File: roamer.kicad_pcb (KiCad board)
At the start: 4 copper layers, 108 parts, among them J1 Conn_Coaxial_Small, J2 JSTPH, J3 Conn_02x05_Odd_Even, J4 Conn_Coaxial_Small, J8 MEM2075-00-140-01-A, Q3 DMP2070UQ-7, SW1 KMR2, U1 2MB Flash, U2 AP2112K-3.3, U3 MCP73831-2-OT, U4 RFM95W-915S2, U5 RFM69W, U6 AP3602AKTR-G1, U7 BME688, U8 INA260, X2 32.768 kHz, X3 microUSB 2.0 B

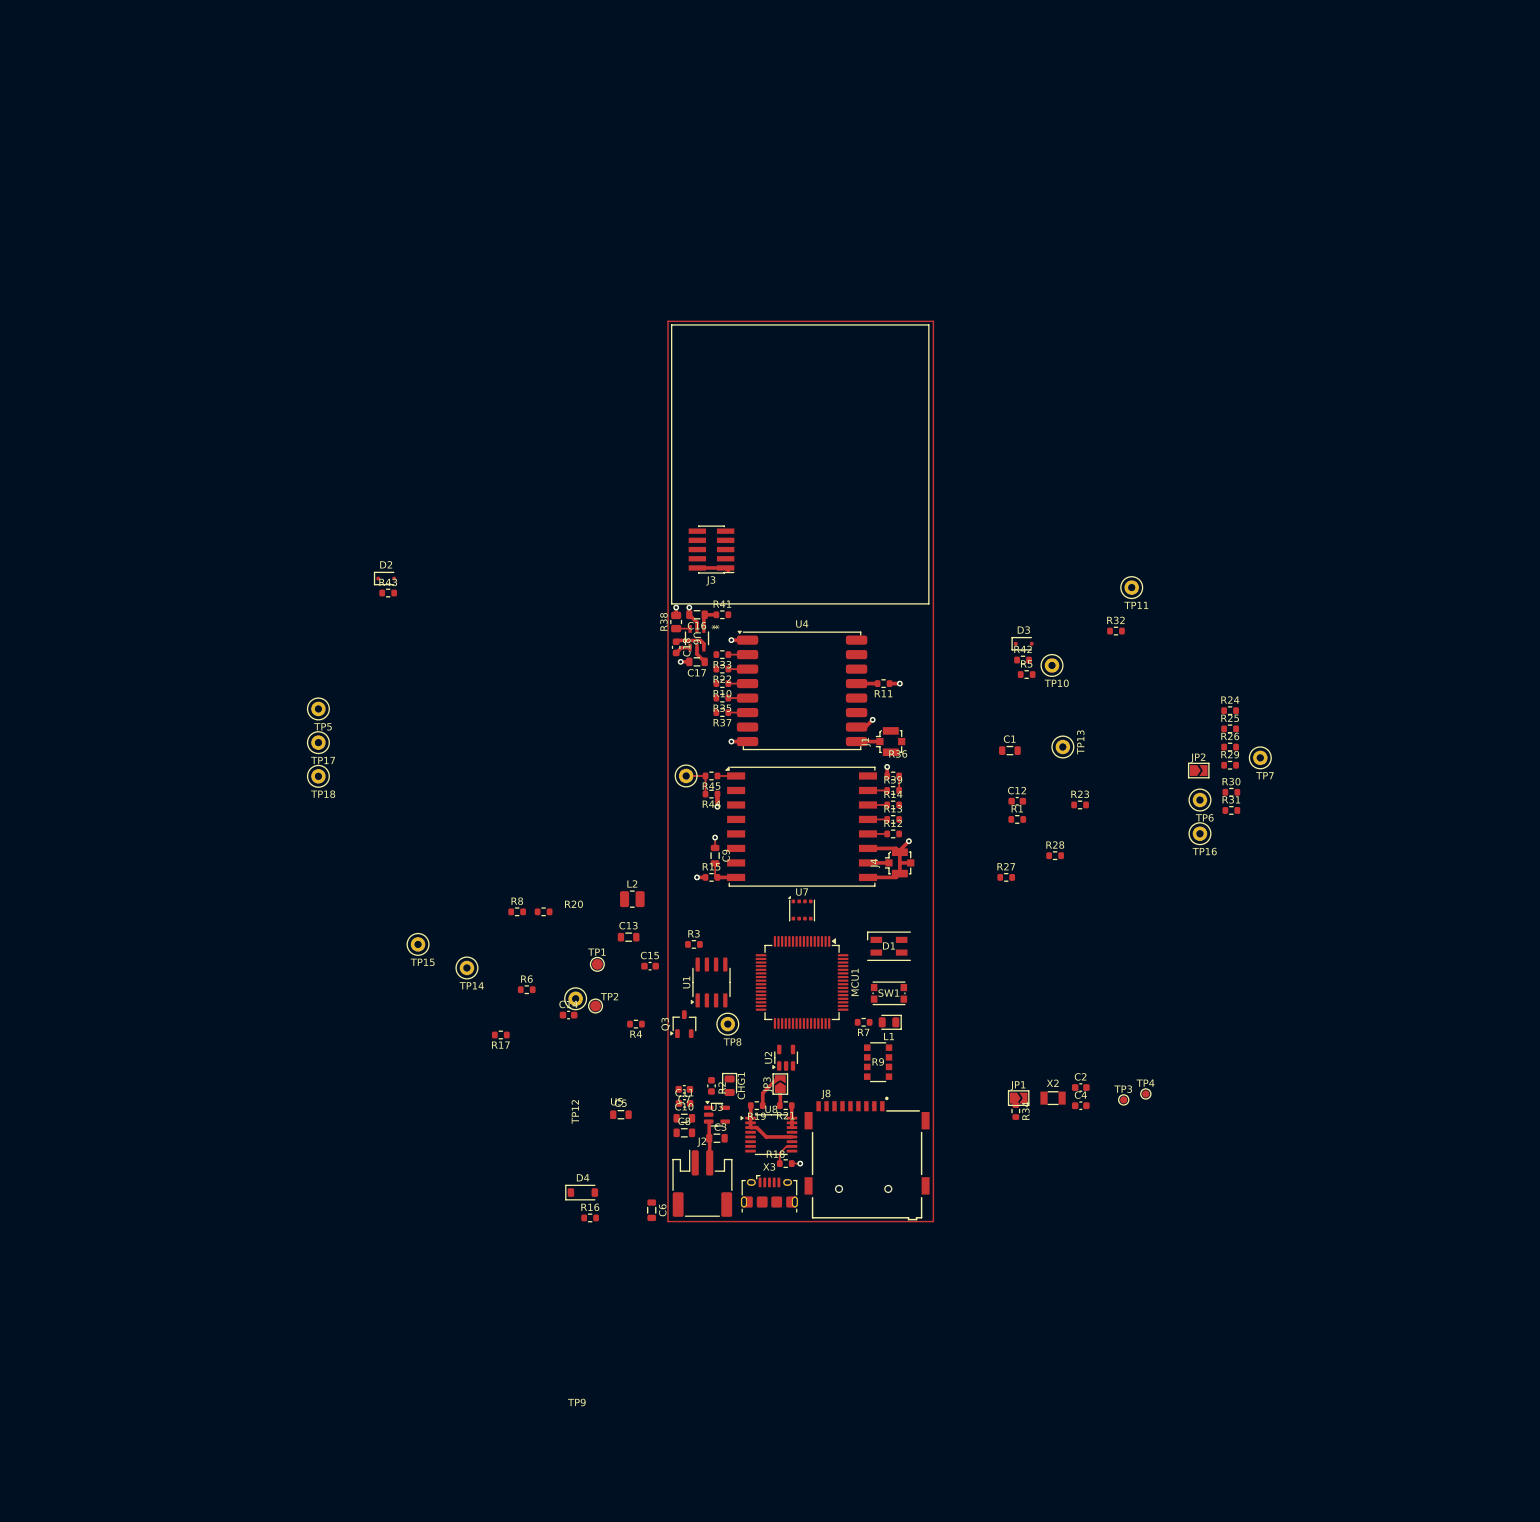
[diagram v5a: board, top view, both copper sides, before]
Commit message: Layed out the radio and PMS00
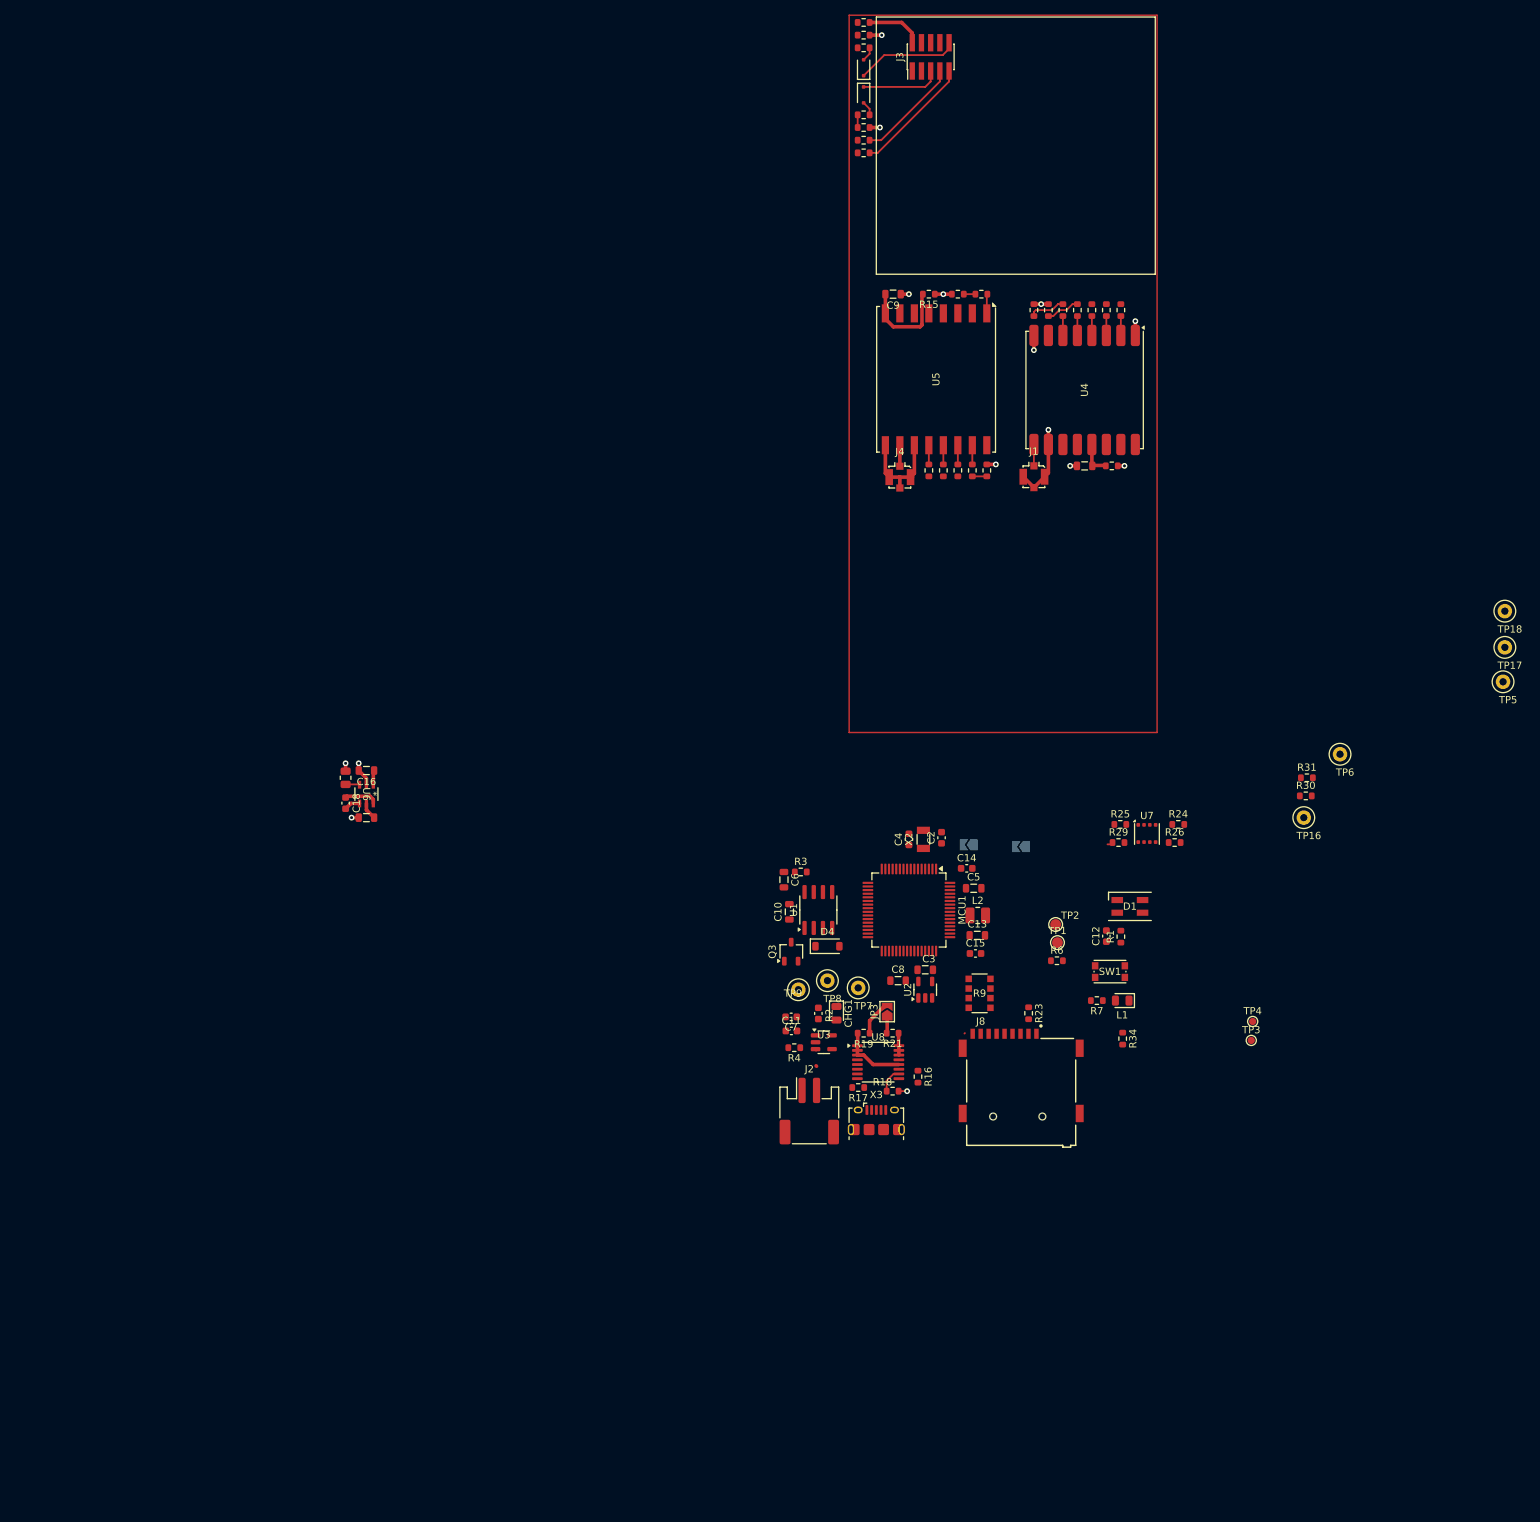
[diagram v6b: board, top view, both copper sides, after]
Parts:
- removed TP10, TP11, TP12, TP13, TP14, TP15: TestPoint, TestPoint:TestPoint_Loop_D2.50mm_Drill1.0mm
- JP1, JP2: moved to B.Cu
- moved TP18 165.3 mm to (307.0, 115.8)
- moved TP17 164.3 mm to (307.0, 120.8)
- moved TP5 163.5 mm to (306.8, 125.5)
- moved R8 110.8 mm to (244.0, 74.2), turned to -90 degrees
- moved R20 107.1 mm to (242.0, 74.2), turned to -90 degrees
- moved R27 103.6 mm to (218.5, 50.8), turned to 180 degrees
- moved R28 100.5 mm to (218.5, 52.5), turned to 180 degrees
- moved D2 93.8 mm to (218.5, 44.5), turned to -90 degrees
- moved R43 93.1 mm to (218.5, 47.2), turned to 180 degrees
- moved R5 91.1 mm to (218.5, 36.2), turned to 180 degrees
- moved R42 87.3 mm to (218.5, 38.0)
- moved R15 85.9 mm to (227.5, 72.0), turned to 180 degrees
- moved R41 84.0 mm to (218.5, 34.5)
- moved D3 82.5 mm to (218.5, 40.8), turned to 90 degrees
- moved C9 81.3 mm to (222.6, 72.0), turned to 180 degrees
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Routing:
- net Net-(J3-Pin_9): track 0.00 -> 16.5 mm
- net Net-(J3-Pin_7): track 0.00 -> 14.5 mm
- net Net-(D3-K): track 0.00 -> 14.2 mm
- net Net-(D2-K): track 0.00 -> 11.0 mm
- net Net-(U5-3.3V): track 4.90 -> 13.3 mm
- net GND: track 28.8 -> 35.4 mm
- net +BATT: track 11.0 -> 5.43 mm
- net /Comms - LoRa 900/~{RESET_LORA_900}: track 0.00 -> 5.02 mm
- net /Comms - LoRa 900/CS_LORA_900: track 0.00 -> 4.68 mm
- net +3V3: track 10.3 -> 14.7 mm, vias 6 -> 8
- net /Comms - LoRa 433/~{RESET_LORA_433}: track 5.18 -> 1.60 mm
- net Net-(J3-Pin_1): track 4.43 -> 7.83 mm
- net Net-(U4-3.3V): track 2.90 -> 5.02 mm
- net Net-(D3-A): track 0.00 -> 1.99 mm
- net Net-(D2-A): track 0.00 -> 1.99 mm
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
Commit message: Working on layout still
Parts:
- added R5: 10K, Resistor_SMD:R_0603_1608Metric, F.Cu at (255.5, 101.8)
- added TP10: TestPoint, TestPoint:TestPoint_Loop_D2.50mm_Drill1.0mm, F.Cu at (245.2, 50.4)
- added TP11: TestPoint, TestPoint:TestPoint_Loop_D2.50mm_Drill1.0mm, F.Cu at (245.2, 55.0)
- added TP12: TestPoint, TestPoint:TestPoint_Loop_D2.50mm_Drill1.0mm, F.Cu at (238.5, 50.4)
- added TP13: TestPoint, TestPoint:TestPoint_Loop_D2.50mm_Drill1.0mm, F.Cu at (238.5, 55.0)
- added TP14: TestPoint, TestPoint:TestPoint_Loop_D2.50mm_Drill1.0mm, F.Cu at (251.8, 50.4)
- added TP15: TestPoint, TestPoint:TestPoint_Loop_D2.50mm_Drill1.0mm, F.Cu at (251.8, 55.0)
- moved C17 89.6 mm to (228.2, 100.8), turned to -90 degrees
- moved C18 88.2 mm to (226.2, 103.6), turned to 180 degrees
- moved TP18 86.2 mm to (238.5, 63.5), turned to 90 degrees
- moved TP17 85.5 mm to (243.5, 63.5), turned to 90 degrees
- moved U6 85.2 mm to (225.0, 100.8), turned to 0 degrees
- moved TP5 85.1 mm to (248.2, 63.8), turned to 90 degrees
- moved R38 83.5 mm to (222.8, 103.6), turned to 180 degrees
- moved C16 80.8 mm to (221.8, 100.8), turned to -90 degrees
- moved C10 77.0 mm to (252.5, 94.2), turned to 0 degrees
- moved R18 75.7 mm to (236.7, 107.6), turned to 90 degrees
- moved U1 71.3 mm to (252.2, 98.0), turned to 180 degrees
- moved R19 68.4 mm to (235.0, 107.6), turned to 90 degrees
- moved U8 66.3 mm to (234.8, 113.2), turned to 90 degrees
- moved U3 64.7 mm to (227.7, 112.2), turned to 180 degrees
- moved R4 63.7 mm to (227.3, 115.0)
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- renumbered R5 to R40
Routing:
- net Net-(D3-K): track 14.2 -> 51.0 mm, vias 0 -> 2
- net Net-(J3-Pin_9): track 16.5 -> 51.6 mm, vias 0 -> 2
- net Net-(J3-Pin_7): track 14.5 -> 49.3 mm, vias 0 -> 2
- net +5V: track 2.24 -> 34.8 mm, vias 0 -> 2
- net Net-(D2-K): track 11.0 -> 42.4 mm, vias 0 -> 2
- net Net-(J3-Pin_1): track 7.83 -> 34.5 mm
- net GND: track 35.4 -> 58.2 mm, vias 7 -> 14
- net +3V3: track 14.7 -> 37.2 mm, vias 8 -> 11
- net /MCU/AIRQ_SET: track 0.10 -> 16.8 mm
- net Net-(D4-K): track 0.00 -> 16.0 mm
- net /MCU - Memory/QSPI.DATA0: track 0.00 -> 8.77 mm, vias 0 -> 3
- net Net-(U8-VBUS): track 9.30 -> 1.99 mm
- net /MCU - Memory/QSPI.SCK: track 0.00 -> 7.25 mm
- net /MCU - Memory/QSPI.DATA2: track 0.00 -> 6.93 mm
- net /MCU/~{AIRQ_RESET}: track 1.75 -> 8.58 mm
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
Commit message: Getting there with the layout
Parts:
- removed TP10, TP11, TP12, TP13, TP14, TP15, TP7, TP8, TP9: TestPoint, TestPoint:TestPoint_Loop_D2.50mm_Drill1.0mm
- JP3: moved to B.Cu
- moved C6 58.4 mm to (189.1, 157.0)
- moved D4 58.4 mm to (194.1, 156.8)
- moved Q3 58.4 mm to (189.1, 160.0)
- moved R3 58.4 mm to (190.0, 162.8)
- moved R4 58.4 mm to (193.8, 162.8)
- moved U2 58.4 mm to (194.1, 165.5)
- moved U3 58.4 mm to (194.1, 160.0)
- moved CHG1 52.9 mm to (186.5, 166.8), turned to 0 degrees
- moved R18 52.3 mm to (219.1, 156.9), turned to -90 degrees
- moved R34 52.1 mm to (216.1, 159.4)
- moved J8 51.9 mm to (223.1, 172.7)
- moved R17 51.8 mm to (217.1, 149.4), turned to 90 degrees
- moved R19 51.2 mm to (220.9, 156.9), turned to -90 degrees
- moved R16 50.5 mm to (217.1, 153.4)
- moved TP6 49.7 mm to (206.4, 151.4)
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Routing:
- net /Bus - SPI/SPI.SCK: track 0.00 -> 82.7 mm, vias 0 -> 4
- net /Bus - SPI/SPI.MISO: track 0.00 -> 69.8 mm, vias 0 -> 4
- net /Bus - SPI/SPI.MOSI: track 0.39 -> 68.5 mm, vias 0 -> 4
- net /Comms - LoRa 433/~{RESET_LORA_433}: track 1.60 -> 47.8 mm, vias 0 -> 2
- net /Comms - LoRa 900/~{RESET_LORA_900}: track 5.02 -> 49.1 mm, vias 0 -> 2
- net /Interface - uUSB/D-: track 0.00 -> 32.7 mm
- net GND: track 58.2 -> 90.2 mm, vias 14 -> 21
- net /Interface - uUSB/D+: track 0.00 -> 28.7 mm
- net /MCU/SWDIO: track 0.00 -> 23.5 mm, vias 0 -> 2
- net /MCU/SWCLK: track 0.00 -> 22.0 mm, vias 0 -> 2
- net /Interface - uSD/CS_uSD: track 0.00 -> 21.1 mm, vias 0 -> 2
- net +3V3: track 37.2 -> 48.5 mm, vias 11 -> 16
- net /MCU/~{RESET}: track 0.00 -> 9.05 mm
- net /MCU/D8_NEOPIX: track 0.00 -> 7.55 mm
- net Net-(MCU1-VSW): track 0.00 -> 7.09 mm
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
